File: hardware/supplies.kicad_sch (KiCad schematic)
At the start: 7 parts, among them U7 LM7805

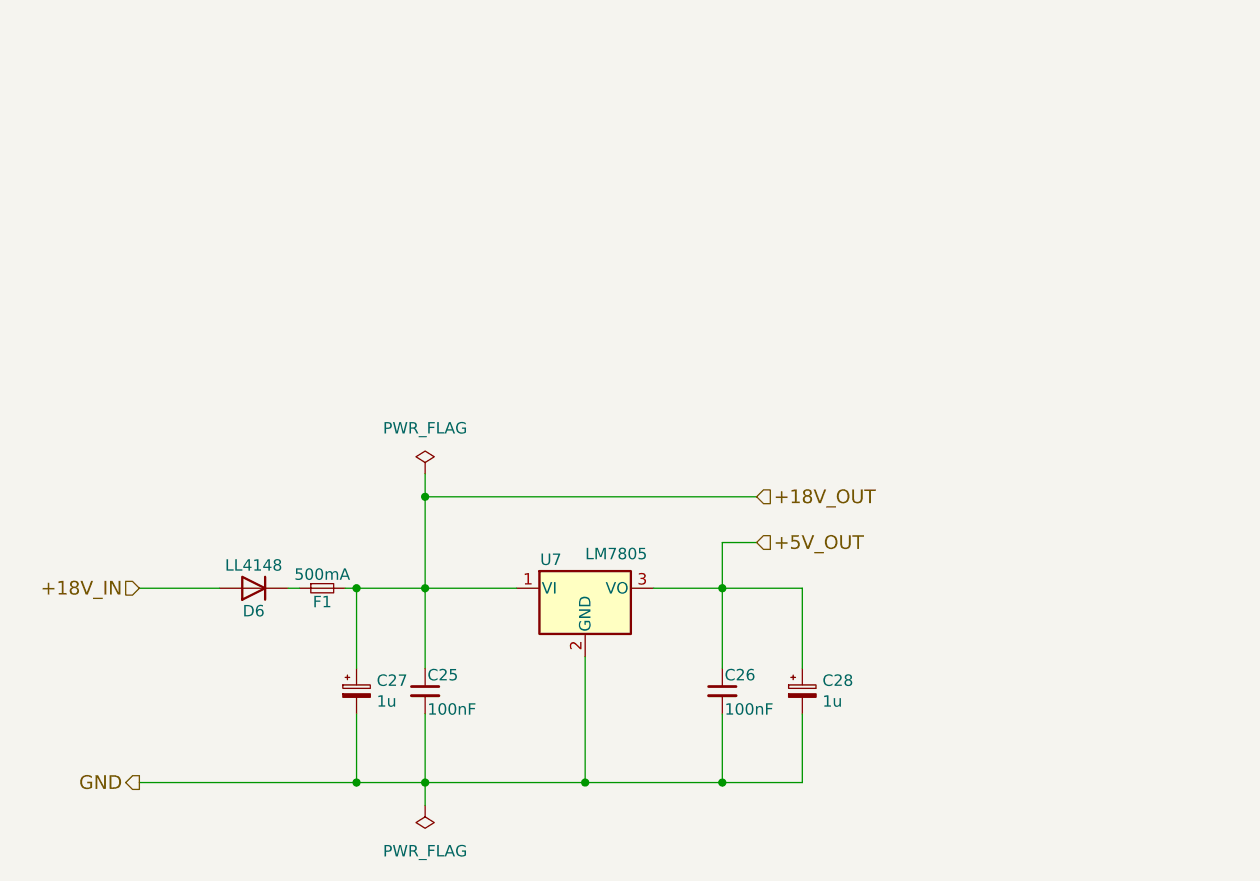
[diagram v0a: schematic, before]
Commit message: Troca do atmega328p -> STM32F103C8T Já que tem CAN integrado e ADC 12 bits (ao invés de 10)
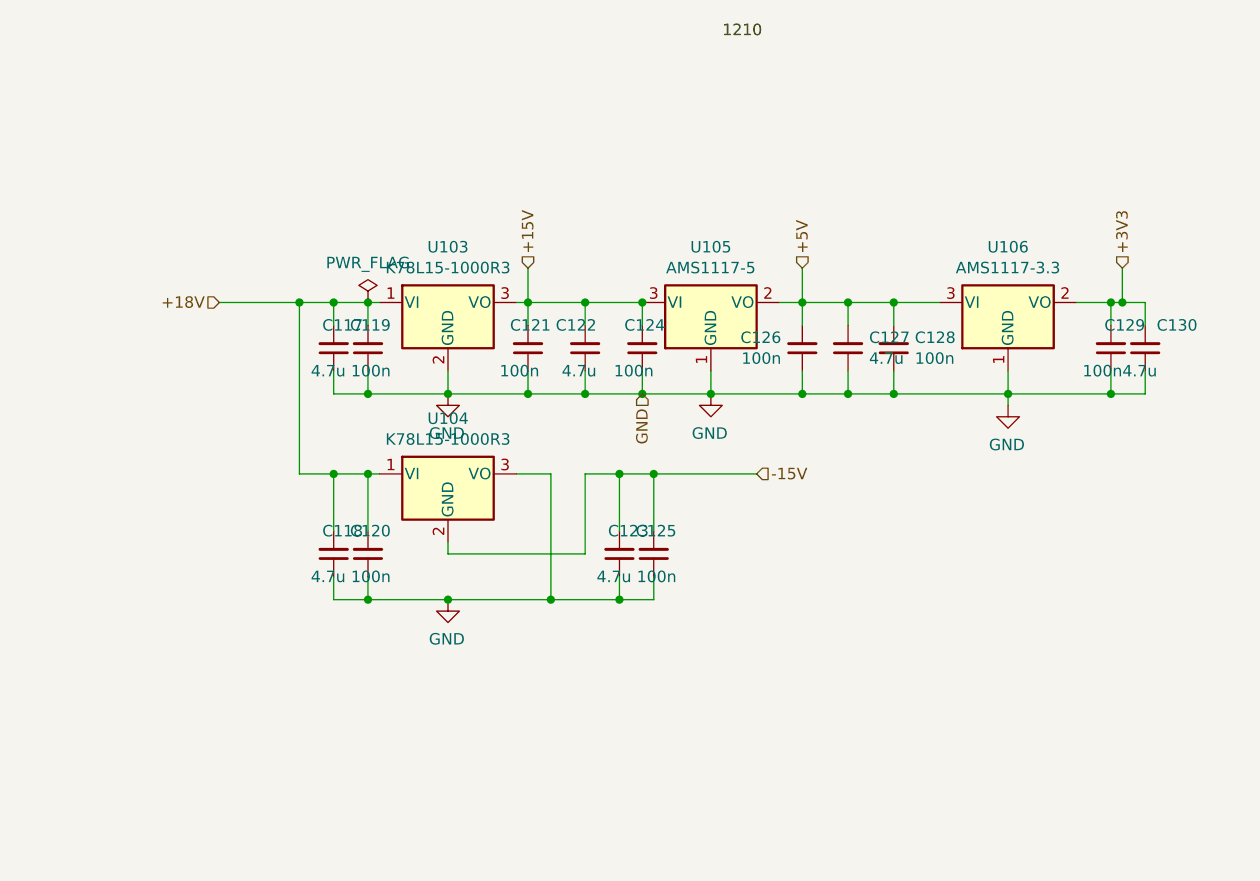
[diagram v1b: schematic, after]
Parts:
- removed C25, C26: 100nF, Capacitor_SMD:C_0805_2012Metric_Pad1.18x1.45mm_HandSolder, symbol Device:C_Small
- removed C27, C28: 1u, Capacitor_Tantalum_SMD:CP_EIA-6032-20_AVX-F_Pad2.25x2.35mm_HandSolder, symbol Device:C_Polarized_Small
- removed D6: LL4148, Diode_SMD:D_MiniMELF_Handsoldering, symbol Diode:LL4148
- removed F1: 500mA, Fuse:Fuse_1206_3216Metric_Pad1.42x1.75mm_HandSolder, symbol Device:Fuse_Small
- removed U7: LM7805, KicadZeniteSolarLibrary18:TO-220-3_Horizontal_TabDown_SMD, symbol Regulator_Linear:LM7805_TO220
- added C117, C118, C122, C123, C127, C130: 4.7u, Capacitor_SMD:C_1206_3216Metric_Pad1.33x1.80mm_HandSolder, symbol Device:C_Small
- added C119, C120, C121, C124, C125, C126, C128, C129: 100n, Capacitor_SMD:C_0603_1608Metric_Pad1.08x0.95mm_HandSolder, symbol Device:C_Small
- added U103, U104: K78L15-1000R3, KicadZeniteSolarLibrary18:TO-220-3_Horizontal_Tabless_SMD, symbol Regulator_Linear:LM7805_TO220
- added U105: AMS1117-5, Package_TO_SOT_SMD:SOT-223-3_TabPin2, symbol Regulator_Linear:AP1117-15
- added U106: AMS1117-3.3, symbol Regulator_Linear:AP1117-15
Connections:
- net GND: now also C117.1, C118.1, C119.1, C120.1, C121.1, C122.1, C123.1, C124.1, C125.1, C126.1, C127.1, C128.1, C129.1, C130.1, U103.2 (GND), U104.3 (VO), U105.1 (GND), U106.1 (GND)
- new net +15V: C121.2, C122.2, C124.2, U103.3 (VO), U105.3 (VI)
- new net +18V: C117.2, C118.2, C119.2, C120.2, U103.1 (VI), U104.1 (VI)
- new net +3V3: C129.2, C130.2, U106.2 (VO)
- new net +5V: C126.2, C127.2, C128.2, U105.2 (VO), U106.3 (VI)
- new net -15V: C123.2, C125.2, U104.2 (GND)

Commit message: Primeiro protótipo da PCB
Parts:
- U106: footprint (none) -> Package_TO_SOT_SMD:SOT-223-3_TabPin2
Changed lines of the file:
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@@
     (property "Reference" "U106" (id 0) (at 196.85 62.4332 0))
     (property "Value" "AMS1117-3.3" (id 1) (at 196.85 64.7446 0))
-    (property "Footprint" "" (id 2) (at 196.85 63.5 0)
+    (property "Footprint" "Package_TO_SOT_SMD:SOT-223-3_TabPin2" (id 2) (at 196.85 63.5 0)
       (effects (font (size 1.27 1.27)) hide)
     )

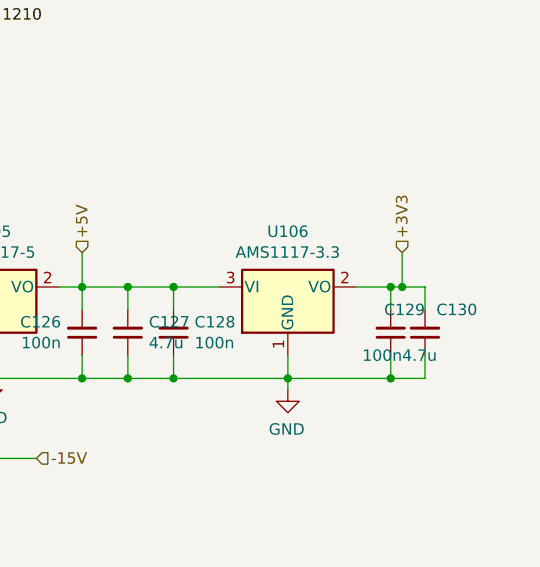
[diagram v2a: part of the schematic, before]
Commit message: STLink 3v3 protection diode, silkscreen updates
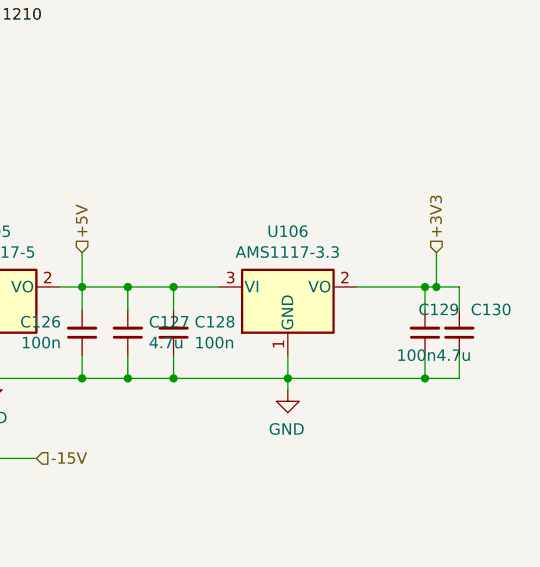
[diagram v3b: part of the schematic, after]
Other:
- moved on the sheet: C129, C130
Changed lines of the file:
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@@
   (junction (at 121.92 87.63) (diameter 0) (color 0 0 0 0)
   )
-  (junction (at 208.28 68.58) (diameter 0) (color 0 0 0 0)
+  (junction (at 212.09 68.58) (diameter 0) (color 0 0 0 0)
   )
   (junction (at 173.99 78.74) (diameter 0) (color 0 0 0 0)
   )
-  (junction (at 208.28 78.74) (diameter 0) (color 0 0 0 0)
-  )
-  (junction (at 209.55 68.58) (diameter 0) (color 0 0 0 0)
+  (junction (at 212.09 78.74) (diameter 0) (color 0 0 0 0)
+  )
+  (junction (at 213.36 68.58) (diameter 0) (color 0 0 0 0)
   )
   (junction (at 163.83 78.74) (diameter 0) (color 0 0 0 0)
@@
     (stroke (width 0) (type default) (color 0 0 0 0))
   )
-  (wire (pts (xy 209.55 68.58) (xy 208.28 68.58))
+  (wire (pts (xy 213.36 68.58) (xy 212.09 68.58))
     (stroke (width 0) (type default) (color 0 0 0 0))
   )
@@
     (stroke (width 0) (type default) (color 0 0 0 0))
   )
+  (wire (pts (xy 196.85 78.74) (xy 212.09 78.74))
+    (stroke (width 0) (type default) (color 0 0 0 0))
+  )
   (wire (pts (xy 121.92 87.63) (xy 121.92 93.98))
     (stroke (width 0) (type default) (color 0 0 0 0))
@@
     (stroke (width 0) (type default) (color 0 0 0 0))
   )
-  (wire (pts (xy 212.09 76.2) (xy 212.09 78.74))
-    (stroke (width 0) (type default) (color 0 0 0 0))
-  )
-  (wire (pts (xy 208.28 78.74) (xy 196.85 78.74))
+  (wire (pts (xy 215.9 76.2) (xy 215.9 78.74))
     (stroke (width 0) (type default) (color 0 0 0 0))
   )
@@
     (stroke (width 0) (type default) (color 0 0 0 0))
   )
-  (wire (pts (xy 212.09 78.74) (xy 208.28 78.74))
-    (stroke (width 0) (type default) (color 0 0 0 0))
-  )
-  (wire (pts (xy 208.28 71.12) (xy 208.28 68.58))
+  (wire (pts (xy 215.9 78.74) (xy 212.09 78.74))
+    (stroke (width 0) (type default) (color 0 0 0 0))
+  )
+  (wire (pts (xy 212.09 71.12) (xy 212.09 68.58))
     (stroke (width 0) (type default) (color 0 0 0 0))
   )
@@
     (stroke (width 0) (type default) (color 0 0 0 0))
   )
-  (wire (pts (xy 208.28 78.74) (xy 208.28 76.2))
+  (wire (pts (xy 212.09 78.74) (xy 212.09 76.2))
     (stroke (width 0) (type default) (color 0 0 0 0))
   )
@@
     (stroke (width 0) (type default) (color 0 0 0 0))
   )
-  (wire (pts (xy 212.09 68.58) (xy 209.55 68.58))
+  (wire (pts (xy 215.9 68.58) (xy 213.36 68.58))
     (stroke (width 0) (type default) (color 0 0 0 0))
   )
@@
     (stroke (width 0) (type default) (color 0 0 0 0))
   )
-  (wire (pts (xy 209.55 64.77) (xy 209.55 68.58))
-    (stroke (width 0) (type default) (color 0 0 0 0))
-  )
-  (wire (pts (xy 212.09 71.12) (xy 212.09 68.58))
+  (wire (pts (xy 213.36 64.77) (xy 213.36 68.58))
+    (stroke (width 0) (type default) (color 0 0 0 0))
+  )
+  (wire (pts (xy 215.9 71.12) (xy 215.9 68.58))
     (stroke (width 0) (type default) (color 0 0 0 0))
   )
@@
     (stroke (width 0) (type default) (color 0 0 0 0))
   )
-  (wire (pts (xy 208.28 68.58) (xy 204.47 68.58))
+  (wire (pts (xy 204.47 68.58) (xy 212.09 68.58))
     (stroke (width 0) (type default) (color 0 0 0 0))
   )
@@
     (effects (font (size 1.27 1.27)) (justify right))
   )
-  (hierarchical_label "+3V3" (shape input) (at 209.55 64.77 90)
+  (hierarchical_label "+3V3" (shape input) (at 213.36 64.77 90)
     (effects (font (size 1.27 1.27)) (justify left))
   )
@@
     (pin "2")
   )
-  (symbol (lib_id "Device:C_Small") (at 212.09 73.66 180) (unit 1)
-    (in_bom yes) (on_board yes)
-    (property "Reference" "C130" (id 0) (at 213.36 71.12 0)
-      (effects (font (size 1.27 1.27)) (justify right))
-    )
-    (property "Value" "4.7u" (id 1) (at 209.55 76.2 0)
-      (effects (font (size 1.27 1.27)) (justify right))
-    )
-    (property "Footprint" "Capacitor_SMD:C_1206_3216Metric_Pad1.33x1.80mm_HandSolder" (id 2) (at 212.09 73.66 0)
-      (effects (font (size 1.27 1.27)) hide)
-    )
-    (property "Datasheet" "~" (id 3) (at 212.09 73.66 0)
+  (symbol (lib_id "Device:C_Small") (at 215.9 73.66 180) (unit 1)
+    (in_bom yes) (on_board yes)
+    (property "Reference" "C130" (id 0) (at 217.17 71.12 0)
+      (effects (font (size 1.27 1.27)) (justify right))
+    )
+    (property "Value" "4.7u" (id 1) (at 213.36 76.2 0)
+      (effects (font (size 1.27 1.27)) (justify right))
+    )
+    (property "Footprint" "Capacitor_SMD:C_1206_3216Metric_Pad1.33x1.80mm_HandSolder" (id 2) (at 215.9 73.66 0)
+      (effects (font (size 1.27 1.27)) hide)
+    )
+    (property "Datasheet" "~" (id 3) (at 215.9 73.66 0)
       (effects (font (size 1.27 1.27)) hide)
     )
@@
     (pin "2")
   )
-  (symbol (lib_id "Device:C_Small") (at 208.28 73.66 0) (mirror x) (unit 1)
-    (in_bom yes) (on_board yes)
-    (property "Reference" "C129" (id 0) (at 212.09 71.12 0)
-      (effects (font (size 1.27 1.27)) (justify right))
-    )
-    (property "Value" "100n" (id 1) (at 209.55 76.2 0)
-      (effects (font (size 1.27 1.27)) (justify right))
-    )
-    (property "Footprint" "Capacitor_SMD:C_0603_1608Metric_Pad1.08x0.95mm_HandSolder" (id 2) (at 208.28 73.66 0)
-      (effects (font (size 1.27 1.27)) hide)
-    )
-    (property "Datasheet" "~" (id 3) (at 208.28 73.66 0)
-      (effects (font (size 1.27 1.27)) hide)
-    )
+  (symbol (lib_id "Device:C_Small") (at 212.09 73.66 0) (mirror x) (unit 1)
+    (in_bom yes) (on_board yes)
+    (property "Reference" "C129" (id 0) (at 215.9 71.12 0)
+      (effects (font (size 1.27 1.27)) (justify right))
+    )
+    (property "Value" "100n" (id 1) (at 213.36 76.2 0)
+      (effects (font (size 1.27 1.27)) (justify right))
+    )
+    (property "Footprint" "Capacitor_SMD:C_0603_1608Metric_Pad1.08x0.95mm_HandSolder" (id 2) (at 212.09 73.66 0)
+      (effects (font (size 1.27 1.27)) hide)
+    )
+    (property "Datasheet" "~" (id 3) (at 212.09 73.66 0)
+      (effects (font (size 1.27 1.27)) hide)
+    )
